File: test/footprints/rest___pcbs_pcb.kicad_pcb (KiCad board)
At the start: 2 copper layers, 19.6 x 14.2 mm, 12 parts, among them J1 Jumper

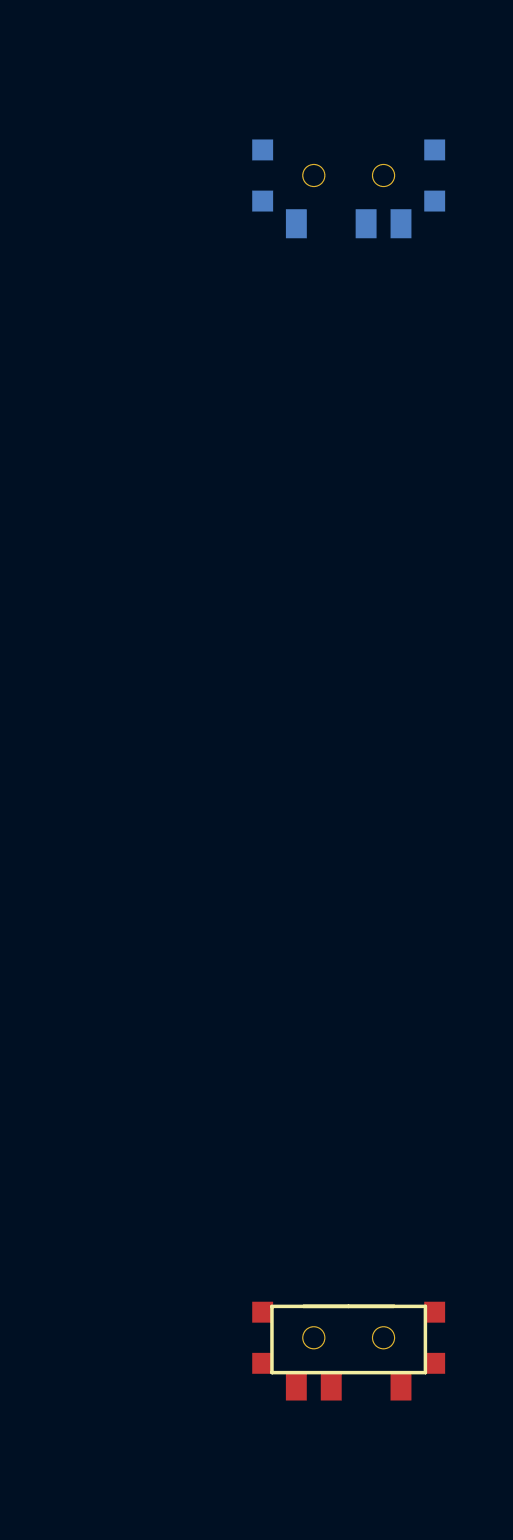
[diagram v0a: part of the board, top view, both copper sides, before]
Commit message: Allow allow slider nets to be referenced
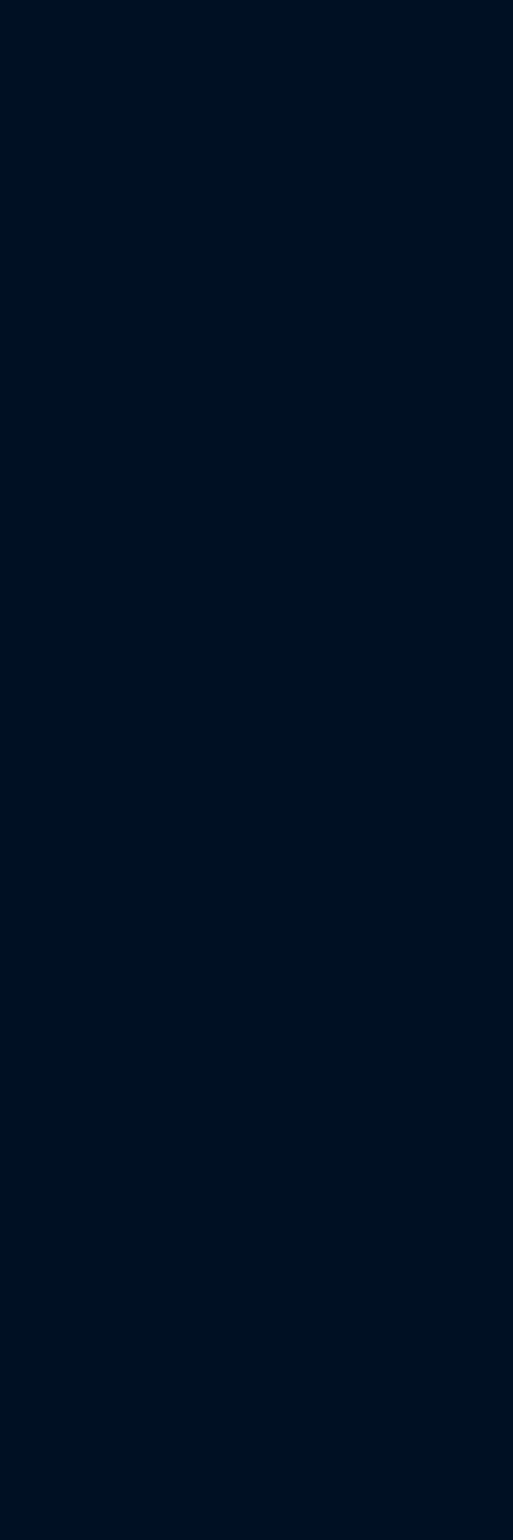
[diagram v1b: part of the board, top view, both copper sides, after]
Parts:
- removed T1, T2: , E73:SPDT_C128955
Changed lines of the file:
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@@
           (pad "" np_thru_hole circle (at -5.625 6.3 0) (size 1.5 1.5) (drill 1.5) (layers *.Cu *.Mask))
-        )
-        (module E73:SPDT_C128955 (layer F.Cu)
-            (at 100 -100 0)
-            (fp_text reference "T1" (at 0 0) (layer F.SilkS) hide (effects (font (size 1.27 1.27) (thickness 0.15))))
-            (fp_text value "" (at 0 0) (layer F.SilkS) hide (effects (font (size 1.27 1.27) (thickness 0.15))))
-            (fp_line (start 1.95 -1.35) (end -1.95 -1.35) (layer F.SilkS) (width 0.15))
-            (fp_line (start 0 -1.35) (end -3.3 -1.35) (layer F.SilkS) (width 0.15))
-            (fp_line (start -3.3 -1.35) (end -3.3 1.5) (layer F.SilkS) (width 0.15))
-            (fp_line (start -3.3 1.5) (end 3.3 1.5) (layer F.SilkS) (width 0.15))
-            (fp_line (start 3.3 1.5) (end 3.3 -1.35) (layer F.SilkS) (width 0.15))
-            (fp_line (start 0 -1.35) (end 3.3 -1.35) (layer F.SilkS) (width 0.15))
-            (fp_line (start -1.95 -3.85) (end 1.95 -3.85) (layer Dwgs.User) (width 0.15))
-            (fp_line (start 1.95 -3.85) (end 1.95 -1.35) (layer Dwgs.User) (width 0.15))
-            (fp_line (start -1.95 -1.35) (end -1.95 -3.85) (layer Dwgs.User) (width 0.15))
-            (pad "" np_thru_hole circle (at 1.5 0) (size 1 1) (drill 0.9) (layers *.Cu *.Mask))
-            (pad "" np_thru_hole circle (at -1.5 0) (size 1 1) (drill 0.9) (layers *.Cu *.Mask))
-            (pad 1 smd rect (at 2.25 2.075 0) (size 0.9 1.25) (layers F.Cu F.Paste F.Mask) (net 1 "from"))
-            (pad 2 smd rect (at -0.75 2.075 0) (size 0.9 1.25) (layers F.Cu F.Paste F.Mask) (net 2 "to"))
-            (pad 3 smd rect (at -2.25 2.075 0) (size 0.9 1.25) (layers F.Cu F.Paste F.Mask))
-            (pad "" smd rect (at 3.7 -1.1 0) (size 0.9 0.9) (layers F.Cu F.Paste F.Mask))
-            (pad "" smd rect (at 3.7 1.1 0) (size 0.9 0.9) (layers F.Cu F.Paste F.Mask))
-            (pad "" smd rect (at -3.7 1.1 0) (size 0.9 0.9) (layers F.Cu F.Paste F.Mask))
-            (pad "" smd rect (at -3.7 -1.1 0) (size 0.9 0.9) (layers F.Cu F.Paste F.Mask))
         )
       (module VIA-0.6mm (layer F.Cu)
@@
           (pad "" np_thru_hole circle (at 5.625 6.3 0) (size 1.5 1.5) (drill 1.5) (layers *.Cu *.Mask))
         )
-        (module E73:SPDT_C128955 (layer F.Cu)
-            (at 100 -150 0)
-            (fp_text reference "T2" (at 0 0) (layer F.SilkS) hide (effects (font (size 1.27 1.27) (thickness 0.15))))
-            (fp_text value "" (at 0 0) (layer F.SilkS) hide (effects (font (size 1.27 1.27) (thickness 0.15))))
-            (fp_line (start 1.95 -1.35) (end -1.95 -1.35) (layer B.SilkS) (width 0.15))
-            (fp_line (start 0 -1.35) (end -3.3 -1.35) (layer B.SilkS) (width 0.15))
-            (fp_line (start -3.3 -1.35) (end -3.3 1.5) (layer B.SilkS) (width 0.15))
-            (fp_line (start -3.3 1.5) (end 3.3 1.5) (layer B.SilkS) (width 0.15))
-            (fp_line (start 3.3 1.5) (end 3.3 -1.35) (layer B.SilkS) (width 0.15))
-            (fp_line (start 0 -1.35) (end 3.3 -1.35) (layer B.SilkS) (width 0.15))
-            (fp_line (start -1.95 -3.85) (end 1.95 -3.85) (layer Dwgs.User) (width 0.15))
-            (fp_line (start 1.95 -3.85) (end 1.95 -1.35) (layer Dwgs.User) (width 0.15))
-            (fp_line (start -1.95 -1.35) (end -1.95 -3.85) (layer Dwgs.User) (width 0.15))
-            (pad "" np_thru_hole circle (at 1.5 0) (size 1 1) (drill 0.9) (layers *.Cu *.Mask))
-            (pad "" np_thru_hole circle (at -1.5 0) (size 1 1) (drill 0.9) (layers *.Cu *.Mask))
-            (pad 1 smd rect (at -2.25 2.075 0) (size 0.9 1.25) (layers B.Cu B.Paste B.Mask) (net 1 "from"))
-            (pad 2 smd rect (at 0.75 2.075 0) (size 0.9 1.25) (layers B.Cu B.Paste B.Mask) (net 2 "to"))
-            (pad 3 smd rect (at 2.25 2.075 0) (size 0.9 1.25) (layers B.Cu B.Paste B.Mask))
-            (pad "" smd rect (at 3.7 -1.1 0) (size 0.9 0.9) (layers B.Cu B.Paste B.Mask))
-            (pad "" smd rect (at 3.7 1.1 0) (size 0.9 0.9) (layers B.Cu B.Paste B.Mask))
-            (pad "" smd rect (at -3.7 1.1 0) (size 0.9 0.9) (layers B.Cu B.Paste B.Mask))
-            (pad "" smd rect (at -3.7 -1.1 0) (size 0.9 0.9) (layers B.Cu B.Paste B.Mask))
-        )
 )
